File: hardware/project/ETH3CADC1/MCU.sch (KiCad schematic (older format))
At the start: 59 parts, among them J501 20021111-00010T4LF, J502 Conn_02x01, U501 SN74LVC1T45DBV, U502 SN74LVC1T45DBV, U503 SN74LVC1T45DBV, U504 HDC1080, U505 MCP2551-I-SN, U506 STM32H743ZI, U507 PCA9517, U508 24LC08B-E/MS, Y501 NX3225GD-8MHZ

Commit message: PCB layout
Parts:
- C514, C518, C519, C521: footprint Capacitor_SMD:C_0603_1608Metric_Pad1.08x0.95mm_HandSolder -> Capacitor_SMD:C_0402_1005Metric_Pad0.74x0.62mm_HandSolder
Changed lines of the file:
@@
 $Descr A2 23386 16535
 encoding utf-8
-Sheet 5 13
+Sheet 5 15
 Title "MCU"
 Date "2020-03-07"
@@
 F 0 "C521" H 8665 10646 50  0000 L CNN
 F 1 "1u" H 8665 10555 50  0000 L CNN
-F 2 "Capacitor_SMD:C_0603_1608Metric_Pad1.08x0.95mm_HandSolder" H 8588 10450 50  0001 C CNN
+F 2 "Capacitor_SMD:C_0402_1005Metric_Pad0.74x0.62mm_HandSolder" H 8588 10450 50  0001 C CNN
 F 3 "~" H 8550 10600 50  0001 C CNN
 	1    8550 10600
@@
 F 0 "C514" H 7365 15496 50  0000 L CNN
 F 1 "1u" H 7365 15405 50  0000 L CNN
-F 2 "Capacitor_SMD:C_0603_1608Metric_Pad1.08x0.95mm_HandSolder" H 7288 15300 50  0001 C CNN
+F 2 "Capacitor_SMD:C_0402_1005Metric_Pad0.74x0.62mm_HandSolder" H 7288 15300 50  0001 C CNN
 F 3 "~" H 7250 15450 50  0001 C CNN
 	1    7250 15450
@@
 F 0 "C519" V 8250 9400 50  0000 C CNN
 F 1 "2u2" V 8250 9750 50  0000 C CNN
-F 2 "Capacitor_SMD:C_0603_1608Metric_Pad1.08x0.95mm_HandSolder" H 8338 9450 50  0001 C CNN
+F 2 "Capacitor_SMD:C_0402_1005Metric_Pad0.74x0.62mm_HandSolder" H 8338 9450 50  0001 C CNN
 F 3 "~" H 8300 9600 50  0001 C CNN
 	1    8300 9600
@@
 F 0 "C518" V 8250 9200 50  0000 C CNN
 F 1 "2u2" V 8250 9550 50  0000 C CNN
-F 2 "Capacitor_SMD:C_0603_1608Metric_Pad1.08x0.95mm_HandSolder" H 8338 9250 50  0001 C CNN
+F 2 "Capacitor_SMD:C_0402_1005Metric_Pad0.74x0.62mm_HandSolder" H 8338 9250 50  0001 C CNN
 F 3 "~" H 8300 9400 50  0001 C CNN
 	1    8300 9400

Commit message: PCB modifications
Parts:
- FB501: footprint Inductor_SMD:L_0805_2012Metric_Pad1.15x1.40mm_HandSolder -> Inductor_SMD:L_0603_1608Metric_Pad1.05x0.95mm_HandSolder
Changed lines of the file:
@@
 F 0 "FB501" V 6726 15250 50  0000 C CNN
 F 1 "742792031" V 6817 15250 50  0000 C CNN
-F 2 "Inductor_SMD:L_0805_2012Metric_Pad1.15x1.40mm_HandSolder" V 6930 15250 50  0001 C CNN
+F 2 "Inductor_SMD:L_0603_1608Metric_Pad1.05x0.95mm_HandSolder" V 6930 15250 50  0001 C CNN
 F 3 "~" H 7000 15250 50  0001 C CNN
 	1    7000 15250

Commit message: PCB modifications
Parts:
- removed C517, C520, C522, C523, C527, C528: 100n, Capacitor_SMD:C_0402_1005Metric_Pad0.74x0.62mm_HandSolder, symbol Device:C
- removed U501, U502, U503: SN74LVC1T45DBV, Package_TO_SOT_SMD:SOT-23-6, symbol Logic_LevelTranslator:SN74LVC1T45DBV
- renumbered C524 to C517, C521 to C520, C525 to C521, C526 to C522, C529 to C523, C530 to C524, U504 to U501, U505 to U502, U506 to U503, U507 to U504, U508 to U505
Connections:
- net labels removed: SD_CLK, SD_DAT, SD_LAT
- wire segments 390 -> 325
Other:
- moved on the sheet: C517, C521, C522

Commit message: SDRAM works, thanks to the website https://medium.com/@pjinwoo123/stm32h7-external-sdram-evaluation-board-cc72444898d8 . Modified the code to work with SDRAM BANK2. SCPI library works.
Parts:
- added RN401, RN402: R_Pack04, Resistor_SMD:R_Array_Concave_4x0402, symbol Device:R_Pack04
- U404: renamed from U504; footprint Package_SO:TSSOP-8_3x3mm_P0.65mm -> Package_SO:MSOP-8_3x3mm_P0.65mm
- renumbered C501 to C401, C502 to C402, C503 to C403, C504 to C404, C505 to C405, C506 to C406, C507 to C407, C508 to C408, C509 to C409, C510 to C410, C511 to C411, C512 to C412, C513 to C413, C514 to C414, C515 to C415, C516 to C416, C517 to C417, C518 to C418, C519 to C419, C520 to C420, C521 to C421, C522 to C422, C523 to C423, C524 to C424, D501 to D401, D502 to D402, D503 to D403, FB501 to FB401, J501 to J401, J502 to J402, R501 to R401, R502 to R402, R503 to R403, R504 to R404, R505 to R405, R506 to R406, R507 to R407, R508 to R408, R509 to R409, R510 to R410, R511 to R411, R512 to R412, R513 to R413, R514 to R414, U501 to U401, U502 to U402, U503 to U403, U505 to U405, Y501 to Y401
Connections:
- net MCU_MISO: now also RN402.5 (R4.2), RN402.6 (R3.2), RN402.7 (R2.2), RN402.8 (R1.2)
- net MCU_MOSI: now also RN401.5 (R4.2), RN401.6 (R3.2), RN401.7 (R2.2), RN401.8 (R1.2)
- net TRIG_EN: now also U403.7 (PC13,EVENTOUT,RTC_TAMP2,RTC_TS,WKUP5); no longer U403.40 (PA4,SPI1_NSS,I2S1_WS,SPI3_NSS,I2S3_WS,USART2_CK,SPI6_NSS,OTG_HS_SOF,DCMI_HSYNC,LCD_VSYNC,EVENTOUT,ADC1_IN4,ADC2_IN4,DAC_OUT1)
- net TRIG_IN: now also U403.9 (PC15,EVENTOUT,OSC32_OUT); no longer U403.42 (PA6,TIM1_BKIN,TIM3_CH1,TIM8_BKIN,SPI1_MISO,SPI6_MISO,TIM13_CH1,MDIOS_MDC,DCMI_PIXCLK,LCD_G2,EVENTOUT,ADC1_IN6,ADC2_IN6)
- net TRIG_OUT: now also U403.8 (PC14,EVENTOUT,OSC32_IN); no longer U403.41 (PA5,TIM2_CH1,TIM2_ETR,TIM8_CH1N,SPI1_SCK,I2S1_CK,SPI6_SCK,OTG_HS_ULPI_CK,LCD_R4,EVENTOUT,ADC1_IN5,ADC2_IN5,DAC_OUT2)
- net FPGA2_nSS: now reaches U403.116 (PD2,TRACED2,TIM3_ETR,UART5_RX,SDMMC1_CMD,DCMI_D11,EVENTOUT)
- net FPGA3_nSS: now reaches U403.117 (PD3,DFSDM1_CKOUT,SPI2_SCK,I2S2_CK,DFSDM1_DATIN0,USART2_CTS,FMC_CLK,DCMI_D5,LCD_G7,EVENTOUT)
- net MCU_AD_RFS: now reaches U403.98 (PC8,TRACED1,TIM3_CH3,TIM8_CH3,UART5_RTS,USART6_CK,FMC_NE2,FMC_NCE,SDMMC1_D0,DCMI_D2,EVENTOUT)
- net DAC_DIN: no longer names the net of U403.21 (PF9,SPI5_MOSI,SAI1_FS_B,UART7_CTS,TIM14_CH1,QUADSPI_BK1_IO1,EVENTOUT,ADC3_IN7)
- net DAC_LDAC: no longer names the net of U403.22 (PF10,QUADSPI_CLK,DCMI_D11,LCD_DE,EVENTOUT,ADC3_IN8)
- net DAC_SCLK: no longer names the net of U403.19 (PF7,TIM11_CH1,SPI5_SCK,SAI1_MCLK_B,UART7_TX,QUADSPI_BK1_IO2,EVENTOUT,ADC3_IN5)
- net DAC_~SYNC: no longer names the net of U403.18 (PF6,TIM10_CH1,SPI5_NSS,SAI1_SD_B,UART7_RX,QUADSPI_BK1_IO3,EVENTOUT,ADC3_IN4)
- net MCU_CLK renamed FPGAx_SCLK
- net MCU_~CS renamed FPGA1_nSS
- new net FPGA1_MISO: RN402.1 (R1.1)
- new net FPGA1_MOSI: RN401.1 (R1.1)
- no-connect marks 42 -> 49

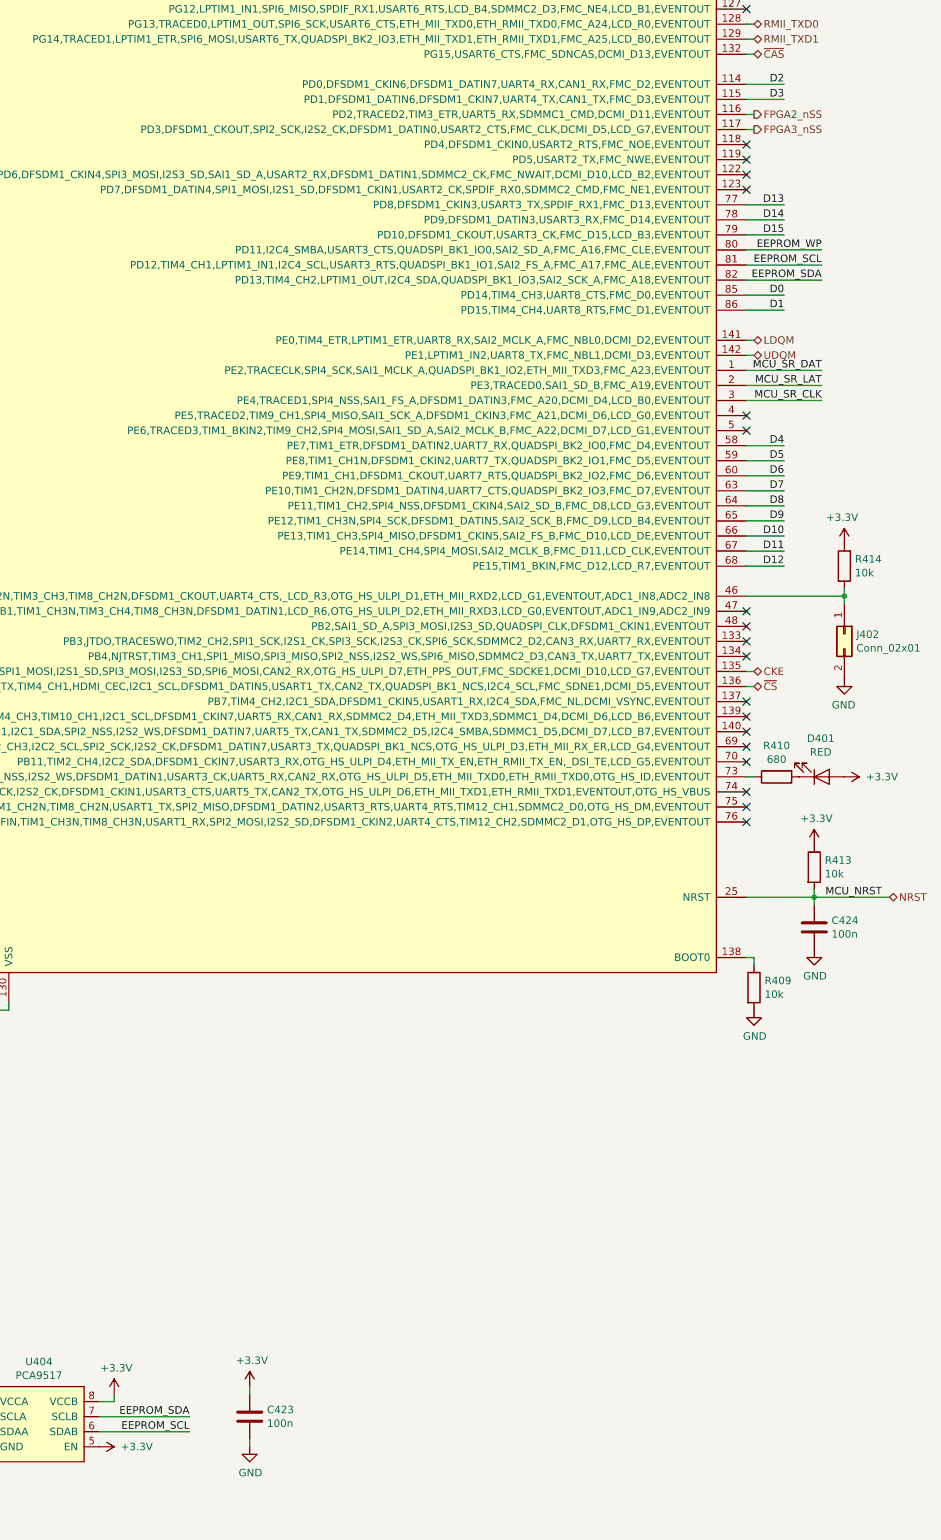
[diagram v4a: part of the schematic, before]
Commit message: Added SDRAM to the linker file.
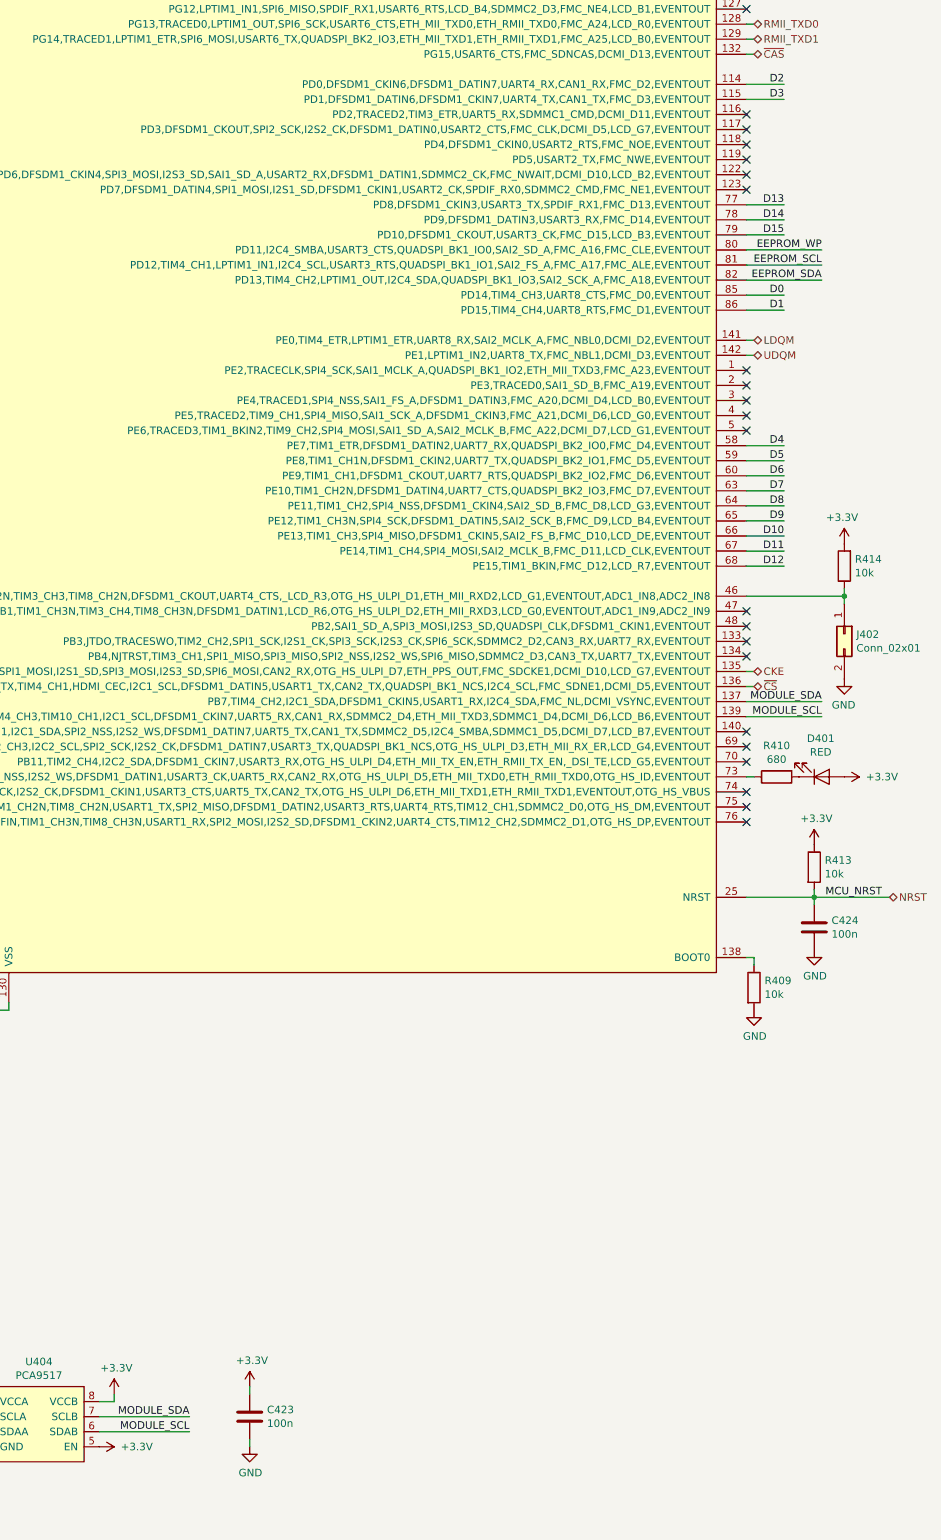
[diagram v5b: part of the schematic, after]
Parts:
- RN401, RN402: footprint Resistor_SMD:R_Array_Concave_4x0402 -> Resistor_SMD:R_Array_Concave_4x0603
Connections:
- net EEPROM_SCL: no longer U404.6 (SDAB)
- net EEPROM_SDA: no longer U404.7 (SCLB)
- net MODULE_SDA: now reaches U403.137 (PB7,TIM4_CH2,I2C1_SDA,DFSDM1_CKIN5,USART1_RX,I2C4_SDA,FMC_NL,DCMI_VSYNC,EVENTOUT)
- net MODULE_SDA: now also U404.7 (SCLB)
- net MODULE_SCL: now reaches U403.139 (PB8,I2C4_SCL,TIM4_CH3,TIM10_CH1,I2C1_SCL,DFSDM1_CKIN7,UART5_RX,CAN1_RX,SDMMC2_D4,ETH_MII_TXD3,SDMMC1_D4,DCMI_D6,LCD_B6,EVENTOUT)
- net MODULE_SCL: now also U404.6 (SDAB)
- net FPGA2_nSS: no longer names the net of U403.116 (PD2,TRACED2,TIM3_ETR,UART5_RX,SDMMC1_CMD,DCMI_D11,EVENTOUT)
- net FPGA3_nSS: no longer names the net of U403.117 (PD3,DFSDM1_CKOUT,SPI2_SCK,I2S2_CK,DFSDM1_DATIN0,USART2_CTS,FMC_CLK,DCMI_D5,LCD_G7,EVENTOUT)
- net MCU_SR_CLK: no longer names the net of U403.3 (PE4,TRACED1,SPI4_NSS,SAI1_FS_A,DFSDM1_DATIN3,FMC_A20,DCMI_D4,LCD_B0,EVENTOUT)
- net MCU_SR_DAT: no longer names the net of U403.1 (PE2,TRACECLK,SPI4_SCK,SAI1_MCLK_A,QUADSPI_BK1_IO2,ETH_MII_TXD3,FMC_A23,EVENTOUT)
- net MCU_SR_LAT: no longer names the net of U403.2 (PE3,TRACED0,SAI1_SD_B,FMC_A19,EVENTOUT)
- no-connect marks 49 -> 52
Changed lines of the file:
@@
 NoConn ~ 20000 4100
 NoConn ~ 20000 8400
-NoConn ~ 20000 8700
-NoConn ~ 20000 8800
 $Comp
 L Device:C C413
@@
 	8550 2600 7700 2600
 Connection ~ 7700 2600
-Wire Wire Line
-	20500 6500 20000 6500
-Text Label 20500 6500 2    50   ~ 0
-MCU_SR_DAT
-Wire Wire Line
-	20000 6700 20500 6700
-Text Label 20500 6700 2    50   ~ 0
-MCU_SR_CLK
-Wire Wire Line
-	20000 6600 20500 6600
-Text Label 20500 6600 2    50   ~ 0
-MCU_SR_LAT
 Text HLabel 8550 7600 0    50   Output ~ 0
 FPGAx_SCLK
@@
 	15800 13350 15800 13300
 Text Label 16300 13450 2    50   ~ 0
-EEPROM_SDA
+MODULE_SDA
 Text Label 16300 13550 2    50   ~ 0
-EEPROM_SCL
+MODULE_SCL
 Wire Wire Line
 	16300 13450 15700 13450
@@
 F 0 "RN402" V 6183 8850 50  0000 C CNN
 F 1 "R_Pack04" V 6274 8850 50  0000 C CNN
-F 2 "Resistor_SMD:R_Array_Concave_4x0402" V 6875 8850 50  0001 C CNN
+F 2 "Resistor_SMD:R_Array_Concave_4x0603" V 6875 8850 50  0001 C CNN
 F 3 "~" H 6600 8850 50  0001 C CNN
 	1    6600 8850
@@
 	6850 8950 6850 8850
 Connection ~ 6850 8850
-Text HLabel 20050 4800 2    50   Output ~ 0
-FPGA2_nSS
-Wire Wire Line
-	20050 4800 20000 4800
-Text HLabel 20050 4900 2    50   Output ~ 0
-FPGA3_nSS
-Wire Wire Line
-	20050 4900 20000 4900
 $Comp
 L Device:R_Pack04 RN401
@@
 F 0 "RN401" V 6183 8150 50  0000 C CNN
 F 1 "R_Pack04" V 6274 8150 50  0000 C CNN
-F 2 "Resistor_SMD:R_Array_Concave_4x0402" V 6875 8150 50  0001 C CNN
+F 2 "Resistor_SMD:R_Array_Concave_4x0603" V 6875 8150 50  0001 C CNN
 F 3 "~" H 6600 8150 50  0001 C CNN
 	1    6600 8150
@@
 NoConn ~ 8600 3900
 NoConn ~ 8600 3800
+Text Label 20500 8700 2    50   ~ 0
+MODULE_SDA
+Text Label 20500 8800 2    50   ~ 0
+MODULE_SCL
+Wire Wire Line
+	20500 8700 20000 8700
+Wire Wire Line
+	20500 8800 20000 8800
+NoConn ~ 20000 6500
+NoConn ~ 20000 6600
+NoConn ~ 20000 6700
+NoConn ~ 20000 4800
+NoConn ~ 20000 4900
 Wire Bus Line
 	6900 5700 6900 7100

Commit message: PCB layout
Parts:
- removed RN401, RN402: R_Pack04, Resistor_SMD:R_Array_Concave_4x0603, symbol Device:R_Pack04
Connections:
- net MCU_MISO is gone; now on net FPGA1_MISO: U403.112 (PC11,DFSDM1_DATIN5,SPI3_MISO,USART3_RX,UART4_RX,QUADSPI_BK2_NCS,SDMMC1_D3,DCMI_D4,EVENTOUT)
- net MCU_MOSI is gone; now on net FPGA1_MOSI: U403.113 (PC12,TRACED3,SPI3_MOSI,I2S3_SD,USART3_CK,UART5_TX,SDMMC1_CK,DCMI_D9,EVENTOUT)
- net MODULE_SCL: now also U403.69 (PB10,TIM2_CH3,I2C2_SCL,SPI2_SCK,I2S2_CK,DFSDM1_DATIN7,USART3_TX,QUADSPI_BK1_NCS,OTG_HS_ULPI_D3,ETH_MII_RX_ER,LCD_G4,EVENTOUT); no longer U403.139 (PB8,I2C4_SCL,TIM4_CH3,TIM10_CH1,I2C1_SCL,DFSDM1_CKIN7,UART5_RX,CAN1_RX,SDMMC2_D4,ETH_MII_TXD3,SDMMC1_D4,DCMI_D6,LCD_B6,EVENTOUT)
- net MODULE_SDA: now also U403.70 (PB11,TIM2_CH4,I2C2_SDA,DFSDM1_CKIN7,USART3_RX,OTG_HS_ULPI_D4,ETH_MII_TX_EN,ETH_RMII_TX_EN,_DSI_TE,LCD_G5,EVENTOUT); no longer U403.137 (PB7,TIM4_CH2,I2C1_SDA,DFSDM1_CKIN5,USART1_RX,I2C4_SDA,FMC_NL,DCMI_VSYNC,EVENTOUT)
- net TRIG_EN: now also U403.42 (PA6,TIM1_BKIN,TIM3_CH1,TIM8_BKIN,SPI1_MISO,SPI6_MISO,TIM13_CH1,MDIOS_MDC,DCMI_PIXCLK,LCD_G2,EVENTOUT,ADC1_IN6,ADC2_IN6); no longer U403.7 (PC13,EVENTOUT,RTC_TAMP2,RTC_TS,WKUP5)
- net TRIG_IN: now also U403.40 (PA4,SPI1_NSS,I2S1_WS,SPI3_NSS,I2S3_WS,USART2_CK,SPI6_NSS,OTG_HS_SOF,DCMI_HSYNC,LCD_VSYNC,EVENTOUT,ADC1_IN4,ADC2_IN4,DAC_OUT1); no longer U403.9 (PC15,EVENTOUT,OSC32_OUT)
- net TRIG_OUT: now also U403.41 (PA5,TIM2_CH1,TIM2_ETR,TIM8_CH1N,SPI1_SCK,I2S1_CK,SPI6_SCK,OTG_HS_ULPI_CK,LCD_R4,EVENTOUT,ADC1_IN5,ADC2_IN5,DAC_OUT2); no longer U403.8 (PC14,EVENTOUT,OSC32_IN)
- net at J402.1 (Pin_1), R414.1: now also U403.48 (PB2,SAI1_SD_A,SPI3_MOSI,I2S3_SD,QUADSPI_CLK,DFSDM1_CKIN1,EVENTOUT); no longer U403.46 (PB0,TIM1_CH2N,TIM3_CH3,TIM8_CH2N,DFSDM1_CKOUT,UART4_CTS,_LCD_R3,OTG_HS_ULPI_D1,ETH_MII_RXD2,LCD_G1,EVENTOUT,ADC1_IN8,ADC2_IN8)
- net at U403.101 (PA9,TIM1_CH2,I2C3_SMBA,SPI2_SCK,I2S2_CK,USART1_TX,DCMI_D0,LCD_R5,EVENTOUT,OTG_FS_VBUS): now also R412.1
- net FPGA2_UART2_TX: now reaches U403.119 (PD5,USART2_TX,FMC_NWE,EVENTOUT)
- net FPGA2_UART2_RX: now reaches U403.122 (PD6,DFSDM1_CKIN4,SPI3_MOSI,I2S3_SD,SAI1_SD_A,USART2_RX,DFSDM1_DATIN1,SDMMC2_CK,FMC_NWAIT,DCMI_D10,LCD_B2,EVENTOUT)
- net at U403.91 (PG6,FMC_NE3,DCMI_D12,LCD_R7,EVENTOUT): no longer R412.1
- net FPGA1_UART6_TX: now reaches U403.96 (PC6,TIM3_CH1,TIM8_CH1,I2S2_MCK,DFSDM1_CKIN3,USART6_TX,FMC_NWAIT,SDMMC2_D6,SDMMC1_D6,DCMI_D0,LCD_HSYNC,EVENTOUT)
- net FPGA1_UART6_RX: now reaches U403.97 (PC7,TIM3_CH2,TIM8_CH2,I2S3_MCK,DFSDM1_DATIN3,USART6_RX,FMC_NE1,SDMMC2_D7,SDMMC1_D7,DCMI_D1,LCD_G6,EVENTOUT)
- no-connect marks 52 -> 42
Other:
- moved on the sheet: D401, D403, R410, R412

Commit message: Development
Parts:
- renumbered D403 to D401, D401 to D403, R412 to R405, R405 to R406, R406 to R407, R407 to R408, R408 to R409, R409 to R410, R413 to R412, R410 to R413
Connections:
- net MCU_AD_RFS: now also U403.1 (PE2,TRACECLK,SPI4_SCK,SAI1_MCLK_A,QUADSPI_BK1_IO2,ETH_MII_TXD3,FMC_A23,EVENTOUT); no longer U403.98 (PC8,TRACED1,TIM3_CH3,TIM8_CH3,UART5_RTS,USART6_CK,FMC_NE2,FMC_NCE,SDMMC1_D0,DCMI_D2,EVENTOUT)
- net FPGA3_UART7_RX: now reaches U403.133 (PB3,JTDO,TRACESWO,TIM2_CH2,SPI1_SCK,I2S1_CK,SPI3_SCK,I2S3_CK,SPI6_SCK,SDMMC2_D2,CAN3_RX,UART7_RX,EVENTOUT)
- net FPGA3_UART7_TX: now reaches U403.134 (PB4,NJTRST,TIM3_CH1,SPI1_MISO,SPI3_MISO,SPI2_NSS,I2S2_WS,SPI6_MISO,SDMMC2_D3,CAN3_TX,UART7_TX,EVENTOUT)
- net FPGA1_MISO renamed FPGAx_MISO
- net FPGA1_MOSI renamed FPGAx_MOSI
- net FPGA1_nSS renamed FPGAx_nSS
- no-connect marks 42 -> 40
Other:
- moved on the sheet: J402, R414
